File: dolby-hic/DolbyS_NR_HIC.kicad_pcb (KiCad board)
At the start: 2 copper layers, 76 x 28 mm, 100 parts, among them J1 DOLBY_S_CONN, Q1 JE, Q2 KD, Q3 JE, Q4 KD, U1 CXA1417Q, U2 M5218

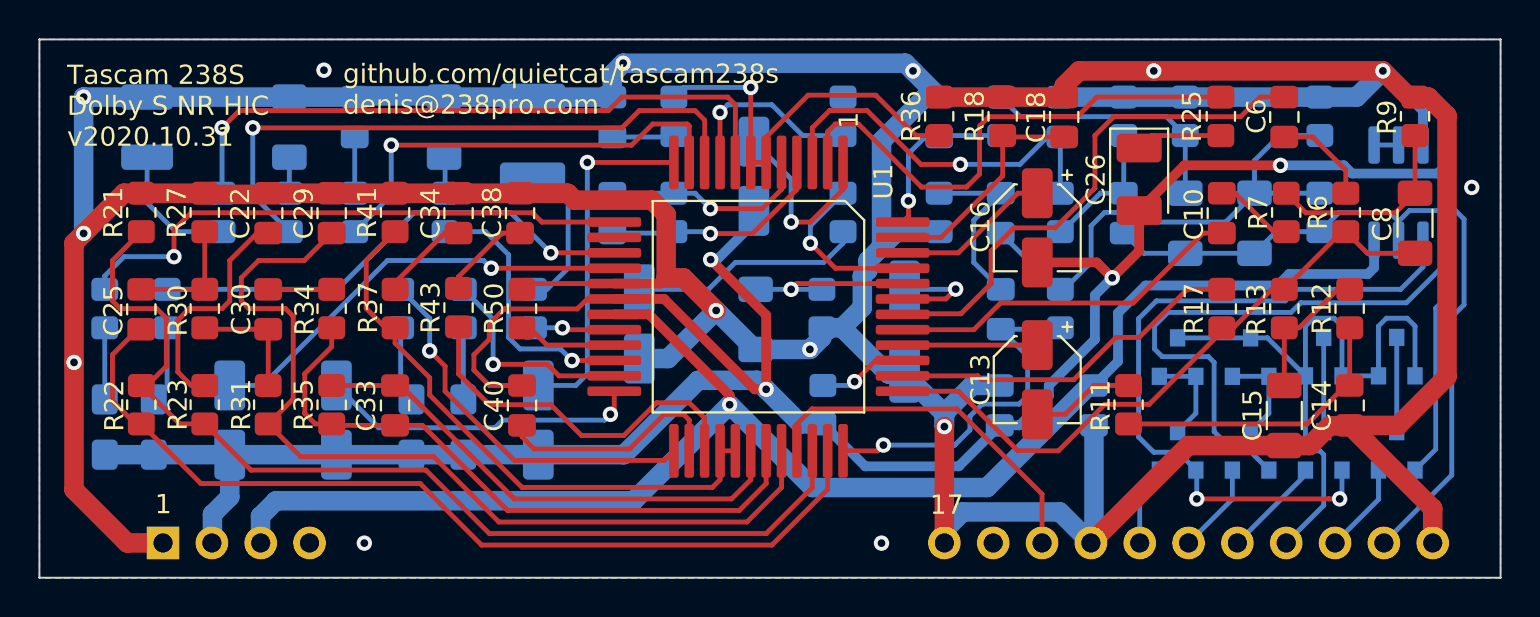
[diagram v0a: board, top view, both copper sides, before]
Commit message: Minor PCB rouing change, eliminated two vias
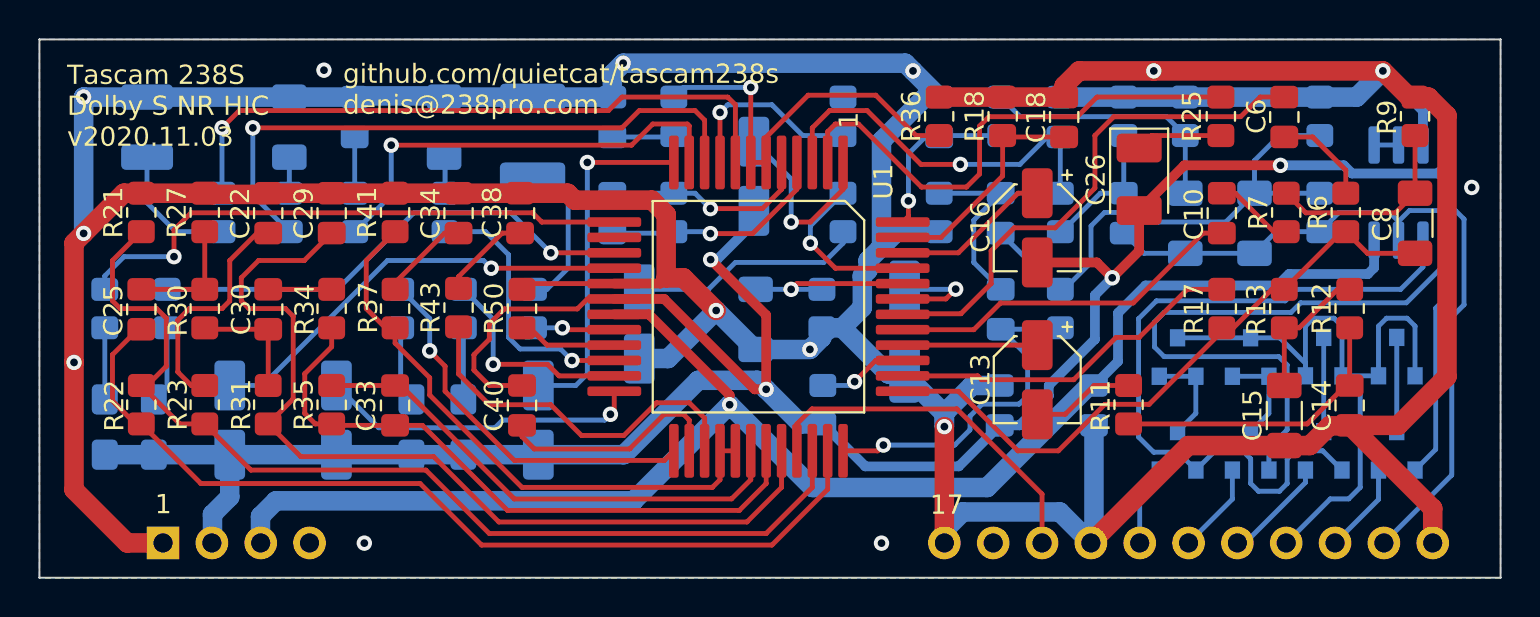
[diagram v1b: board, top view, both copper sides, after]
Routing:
- net Net-(Q1-Pad1): track 41.1 -> 43.6 mm
- net /SEL: track 34.4 -> 35.8 mm
- net Net-(Q3-Pad1): track 37.7 -> 38.9 mm, vias 2 -> 0
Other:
- board text added: "Tascam 238S Dolby S NR HIC v2020.11.03"
- board text removed: "Tascam 238S Dolby S NR HIC v2020.10.31"

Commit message: dolby-hic PCB version 2021.01.10 - moved all electrolytical caps to the back of the board; both chips and input switching transistors on the front
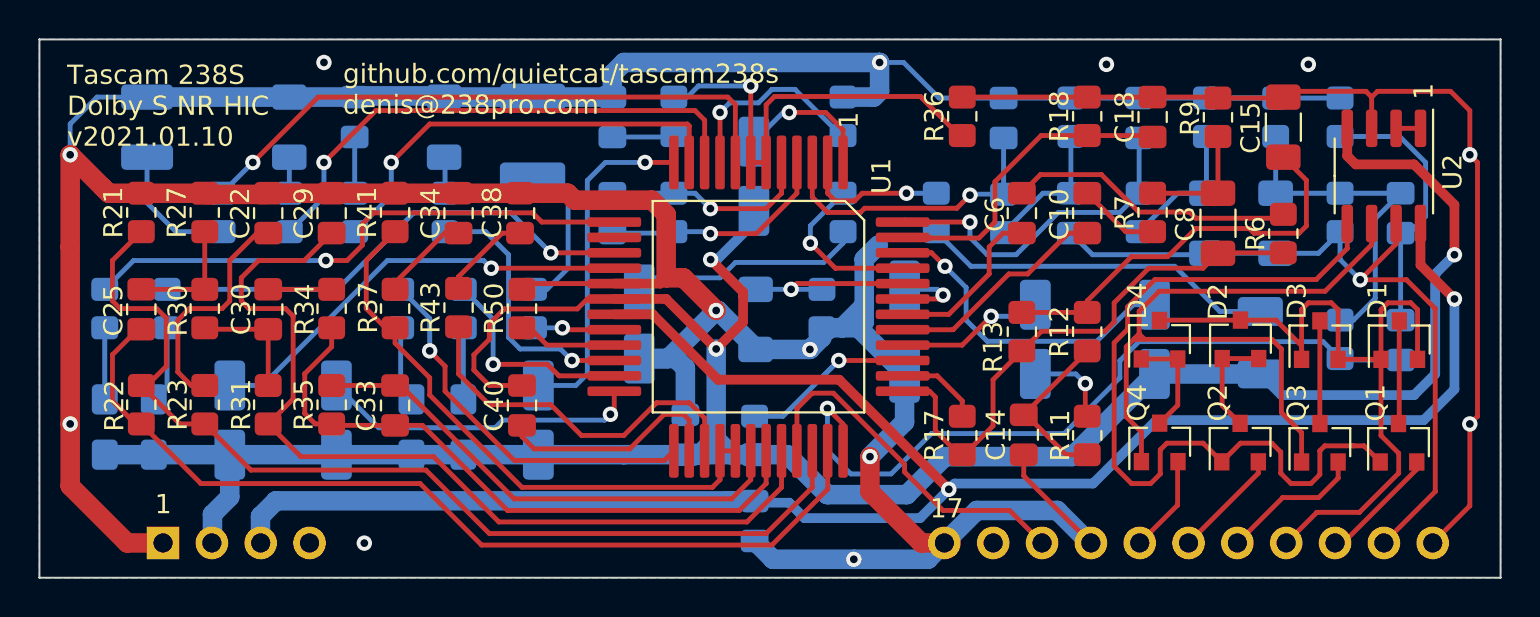
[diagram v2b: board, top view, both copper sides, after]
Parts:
- C13, C16, C26, R25: moved to B.Cu
- D1, D2, D3, D4, Q1, Q2, Q3, Q4, U2: moved to F.Cu
- moved R15 21.4 mm to (199.7, 101.0), turned to 270 degrees
- moved C21 20.9 mm to (202.8, 112.6)
- moved C19 20.8 mm to (202.8, 106.0), turned to 270 degrees
- moved C1 18.6 mm to (169.2, 122.0)
- moved C14 17.0 mm to (183.2, 117.6)
- moved C2 16.4 mm to (165.6, 117.6)
- moved R25 15.6 mm to (178.7, 106.0)
- moved R17 15.0 mm to (180.0, 117.6)
- moved C15 15.0 mm to (196.7, 101.6), turned to 90 degrees
- moved R20 14.6 mm to (199.7, 112.6)
- moved C6 14.5 mm to (183.1, 106.0), turned to 90 degrees
- moved R12 13.7 mm to (186.5, 112.2)
- moved R13 13.7 mm to (183.1, 112.2), turned to 270 degrees
- moved C26 10.6 mm to (195.5, 112.8)
- moved C20 10.4 mm to (189.2, 101.1)
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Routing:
- net Net-(C21-Pad1): track 18.5 -> 38.8 mm
- net Net-(R25-Pad1): track 27.0 -> 7.58 mm, vias 0 -> 1
- net Net-(C6-Pad1): track 27.1 -> 8.77 mm
- net VCC: track 79.4 -> 97.5 mm, vias 1 -> 2
- net GND: track 277.8 -> 262.7 mm, vias 14 -> 13
- net Net-(R17-Pad1): track 18.6 -> 4.44 mm
- net Net-(C15-Pad1): track 7.23 -> 21.3 mm
- net Net-(C26-Pad1): track 4.52 -> 18.6 mm
- net Net-(C6-Pad2): track 5.11 -> 15.0 mm
- net Net-(C16-Pad1): track 8.28 -> 17.9 mm, vias 0 -> 1
- net Net-(C11-Pad2): track 27.0 -> 17.8 mm
- net Net-(C20-Pad1): track 8.87 -> 17.8 mm
- net Net-(C10-Pad1): track 18.7 -> 11.7 mm
- net Net-(C14-Pad1): track 15.3 -> 8.85 mm
- net Net-(C17-Pad2): track 13.4 -> 7.28 mm
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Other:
- board text added: "JLCJLCJLCJLC"
- board text added: "Tascam 238S Dolby S NR HIC v2021.01.10"
- board text removed: "Tascam 238S Dolby S NR HIC v2020.11.03"

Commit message: Updated HIC layout; RP amp clarification
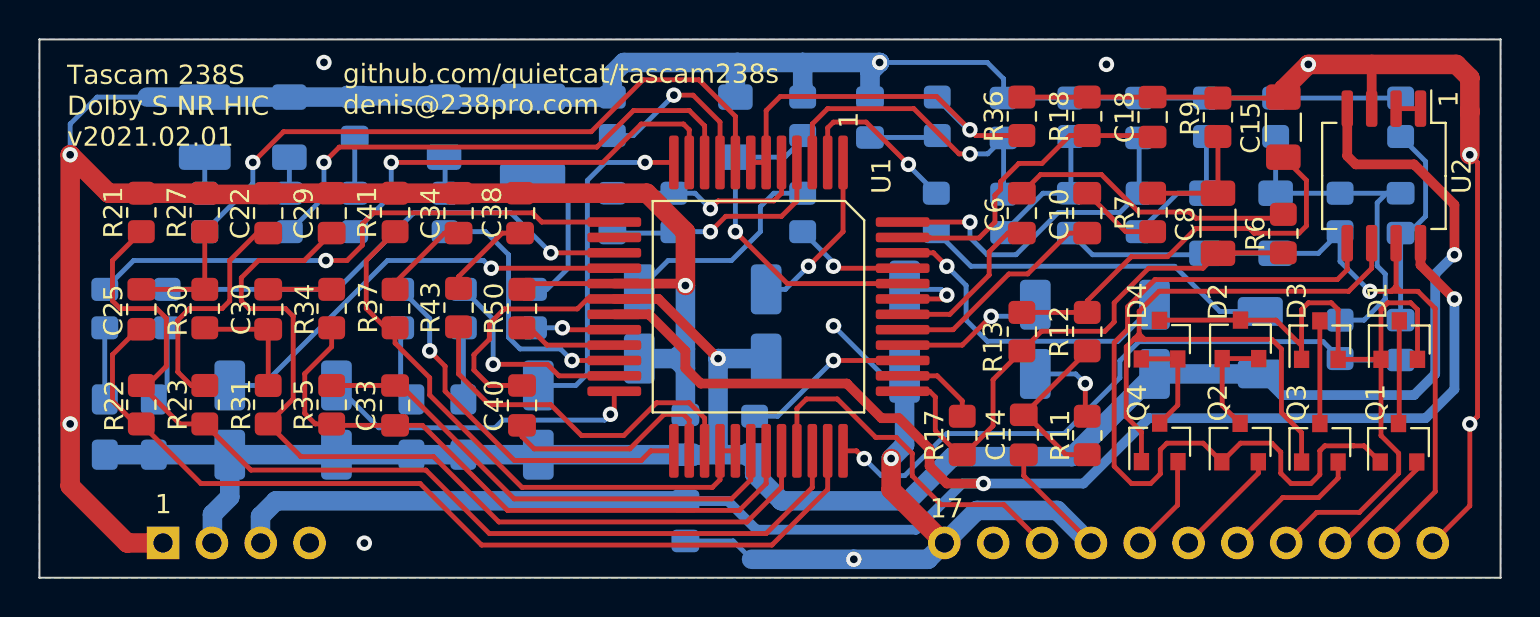
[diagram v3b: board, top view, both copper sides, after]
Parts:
- D1: value D_223 -> MMBD914
- D2, D3, D4: value D -> MMBD914
- Q1, Q3: value JE -> MMBFJ270
- Q2, Q4: value KD -> MMBFJ201
- U2: value M5218 -> NE5532A; footprint Package_SO:SOIC-8_3.9x4.9mm_P1.27mm -> Package_SO:SO-8_5.3x6.2mm_P1.27mm
- moved R32 13.7 mm to (178.7, 101.0)
- moved C31 13.4 mm to (175.2, 101.1)
- moved R40 12.0 mm to (161.8, 101.0)
- moved C7 10.1 mm to (168.2, 101.6), turned to 90 degrees
- moved R8 10.0 mm to (171.7, 101.0), turned to 90 degrees
- moved C23 7.71 mm to (169.8, 111.8)
- moved C1 3.60 mm to (165.6, 122.0)
- moved R15 3.15 mm to (202.8, 101.0)
- moved R36 3.10 mm to (183.1, 101.0)
- moved C35 3.00 mm to (140.6, 101.6)
- moved R52 2.10 mm to (171.7, 106.0), turned to 90 degrees
- moved R38 0.90 mm to (140.6, 106.0), turned to 270 degrees
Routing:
- net Net-(C7-Pad1): track 9.37 -> 17.8 mm
- net VEE: track 132.2 -> 125.2 mm, vias 3 -> 2
- net GND: track 262.7 -> 255.8 mm
- net Net-(C21-Pad1): track 38.8 -> 33.3 mm
- net Net-(C35-Pad2): track 6.90 -> 1.88 mm
- net Net-(C19-Pad2): track 14.0 -> 10.9 mm
- net /Dolby S Encoder/N1: track 23.2 -> 20.4 mm
- net Net-(R38-Pad2): track 31.9 -> 34.7 mm
- net Net-(R52-Pad1): track 8.64 -> 6.10 mm
- net VCC: track 97.5 -> 99.7 mm
- net Net-(R25-Pad1): track 7.58 -> 9.14 mm
- net Net-(C23-Pad1): track 7.34 -> 8.84 mm
- net Net-(R40-Pad2): track 10.5 -> 9.15 mm
- net Net-(C27-Pad1): track 15.6 -> 16.7 mm
- net Net-(C11-Pad2): track 17.8 -> 18.9 mm
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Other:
- board text added: "Tascam 238S Dolby S NR HIC v2021.02.01"
- board text removed: "Tascam 238S Dolby S NR HIC v2021.01.10"
